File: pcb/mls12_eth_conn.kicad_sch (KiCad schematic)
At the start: 12 parts, among them J1 MTJ-88ARX1-FSM-LG

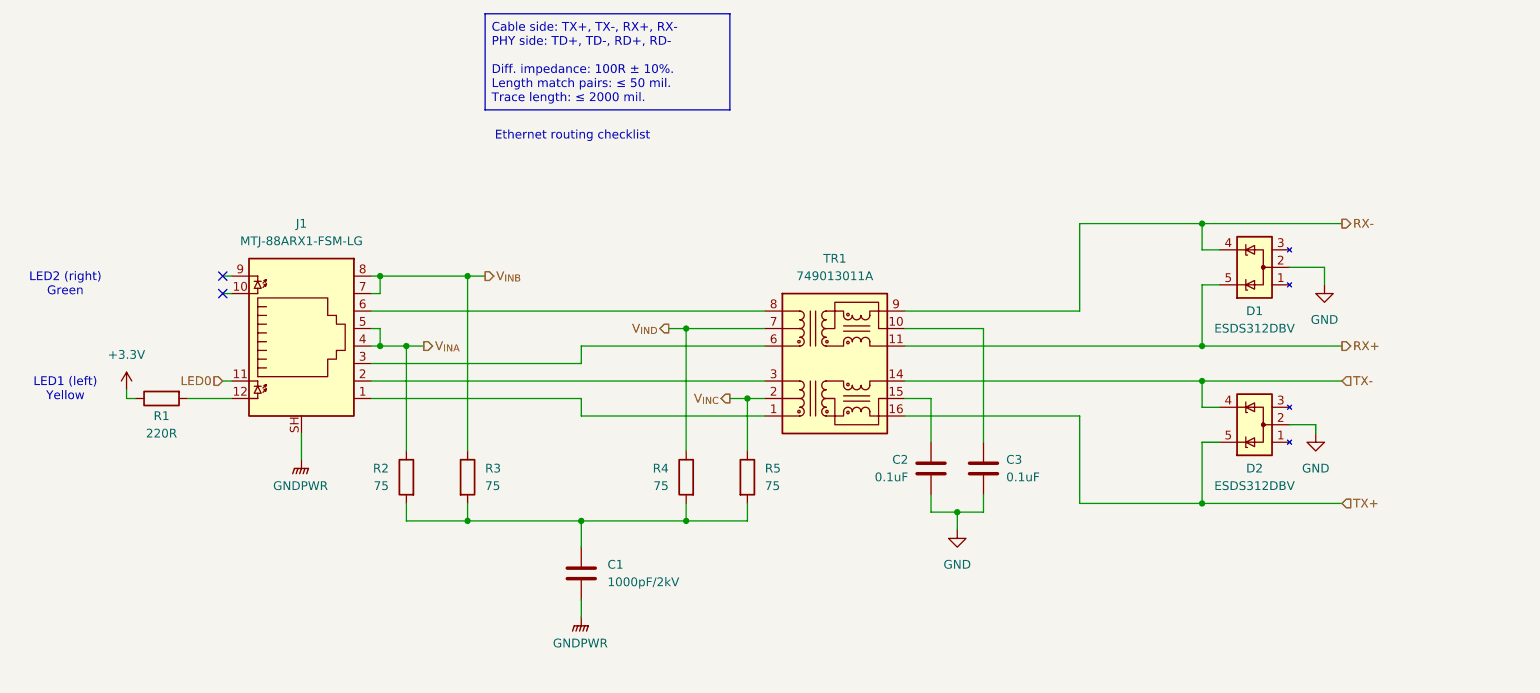
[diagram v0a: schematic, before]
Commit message: Update to 25W PoE+ module, 2 outputs
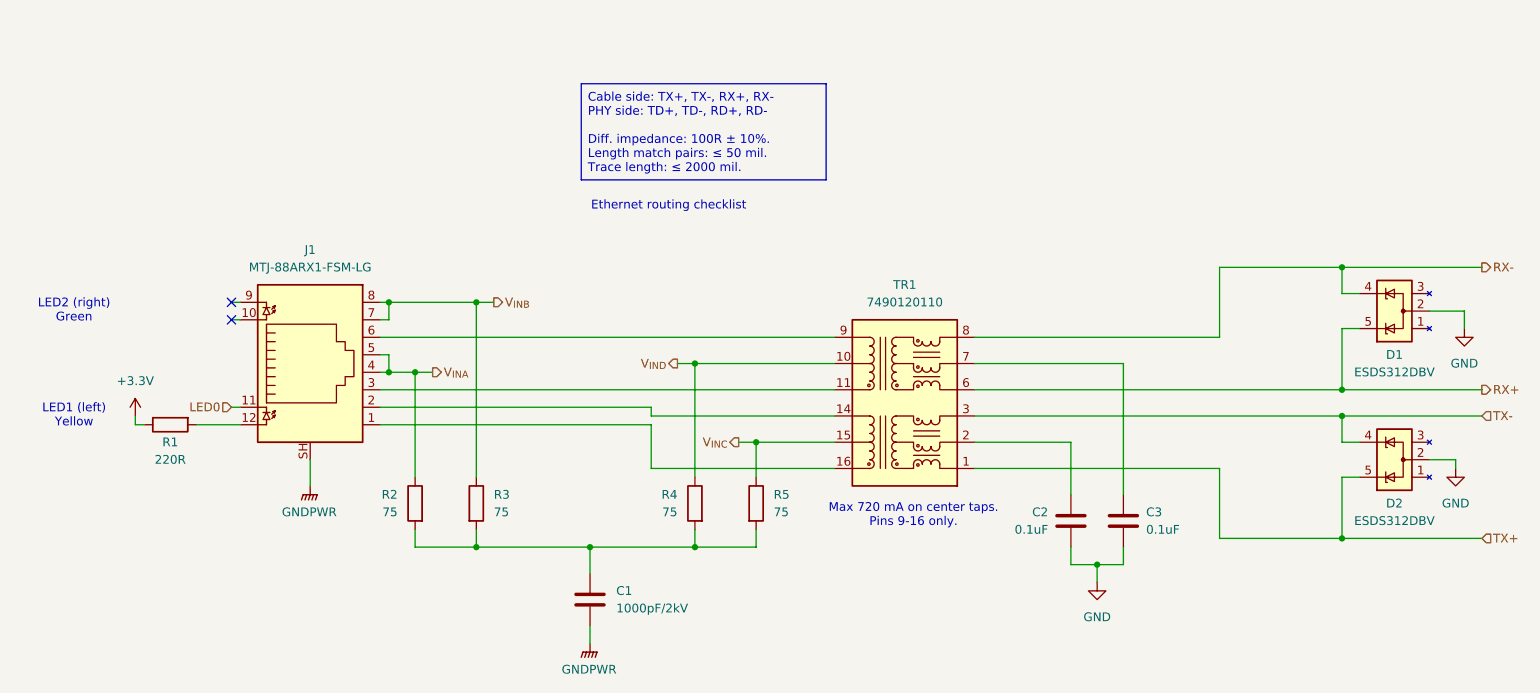
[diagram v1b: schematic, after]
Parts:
- removed TR1: 749013011A, Transformer_SMD:Transformer_Ethernet_Wuerth_749013011A, symbol Transformer:Wuerth_749013011A
- added TR1: 7490120110, symbol mls12:7490120110
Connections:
- net RX+: now also TR1.6 (RD+)
- net RX-: now also TR1.8 (RD-)
- net TX+: now also TR1.1 (TD+)
- net TX-: now also TR1.3 (TD-)
- net V_{INC}: now also TR1.15 (CTX)
- net V_{IND}: now also TR1.10 (CRX)
- net at C2.1: now also TR1.2 (CTD)
- net at C3.1: now also TR1.7 (CRD)
- net at J1.1: now also TR1.16 (TX+)
- net at J1.2: now also TR1.14 (TX-)
- net at J1.3: now also TR1.11 (RX+)
- net at J1.6: now also TR1.9 (RX-)
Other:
- note added: "Max 720 mA on center taps. Pins 9-16 only."
- company: (none) -> Quomodo BV
- moved on the sheet: C1, C2, C3, D1, D2, J1, R1, R2, R3, R4, R5

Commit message: Fix default footprint for PoE+ magnetics
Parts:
- TR1: footprint (none) -> mls12:7490120110
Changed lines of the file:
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@@
 			)
 		)
-		(property "Footprint" ""
+		(property "Footprint" "mls12:7490120110"
 			(at 163.83 82.55 0)
 			(effects

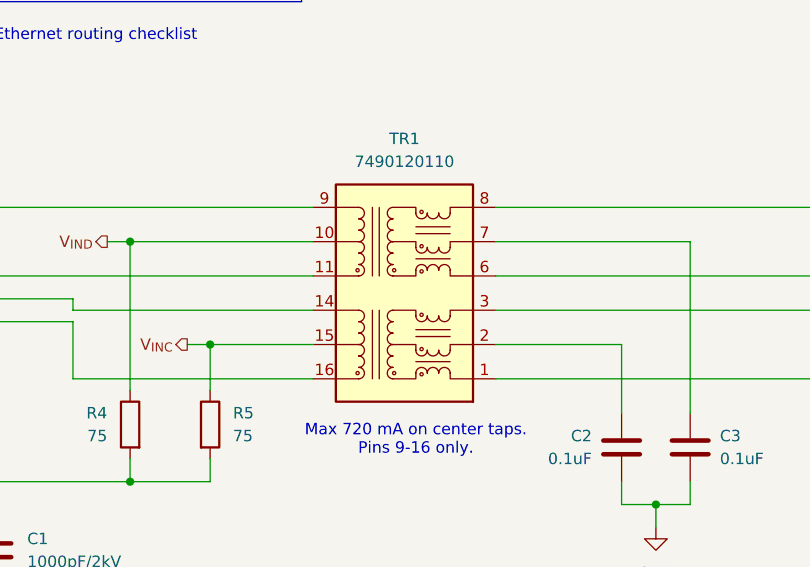
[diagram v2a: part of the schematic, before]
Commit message: First Ethernet frontend layout
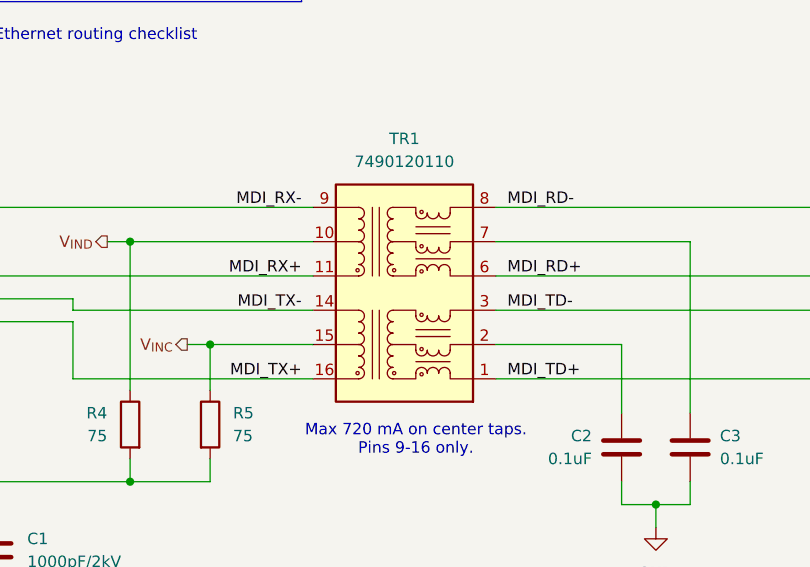
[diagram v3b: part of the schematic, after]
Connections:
- net MDI_TX+: now reaches J1.1, TR1.16 (TX+)
- net MDI_TX-: now reaches J1.2, TR1.14 (TX-)
- net MDI_RX+: now reaches J1.3, TR1.11 (RX+)
- net MDI_RX-: now reaches J1.6, TR1.9 (RX-)
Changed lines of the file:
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@@
+		)
+	)
+	(label "MDI_TD+"
+		(at 175.26 105.41 0)
+		(effects
+			(font
+				(size 1.27 1.27)
+			)
+			(justify left bottom)
+		)
+	)
+	(label "MDI_RD-"
+		(at 175.26 86.36 0)
+		(effects
+			(font
+				(size 1.27 1.27)
+			)
+			(justify left bottom)
+		)
+	)
+	(label "MDI_RD+"
+		(at 175.26 93.98 0)
+		(effects
+			(font
+				(size 1.27 1.27)
+			)
+			(justify left bottom)
+		)
+	)
+	(label "MDI_TD-"
+		(at 175.26 97.79 0)
+		(effects
+			(font
+				(size 1.27 1.27)
+			)
+			(justify left bottom)
+		)
+	)
+	(label "MDI_TX+"
+		(at 152.4 105.41 180)
+		(effects
+			(font
+				(size 1.27 1.27)
+			)
+			(justify right bottom)
+		)
+	)
+	(label "MDI_RX-"
+		(at 152.4 86.36 180)
+		(effects
+			(font
+				(size 1.27 1.27)
+			)
+			(justify right bottom)
+		)
+	)
+	(label "MDI_RX+"
+		(at 152.4 93.98 180)
+		(effects
+			(font
+				(size 1.27 1.27)
+			)
+			(justify right bottom)
+		)
+	)
+	(label "MDI_TX-"
+		(at 152.4 97.79 180)
+		(effects
+			(font
+				(size 1.27 1.27)
+			)
+			(justify right bottom)
 		)
 	)

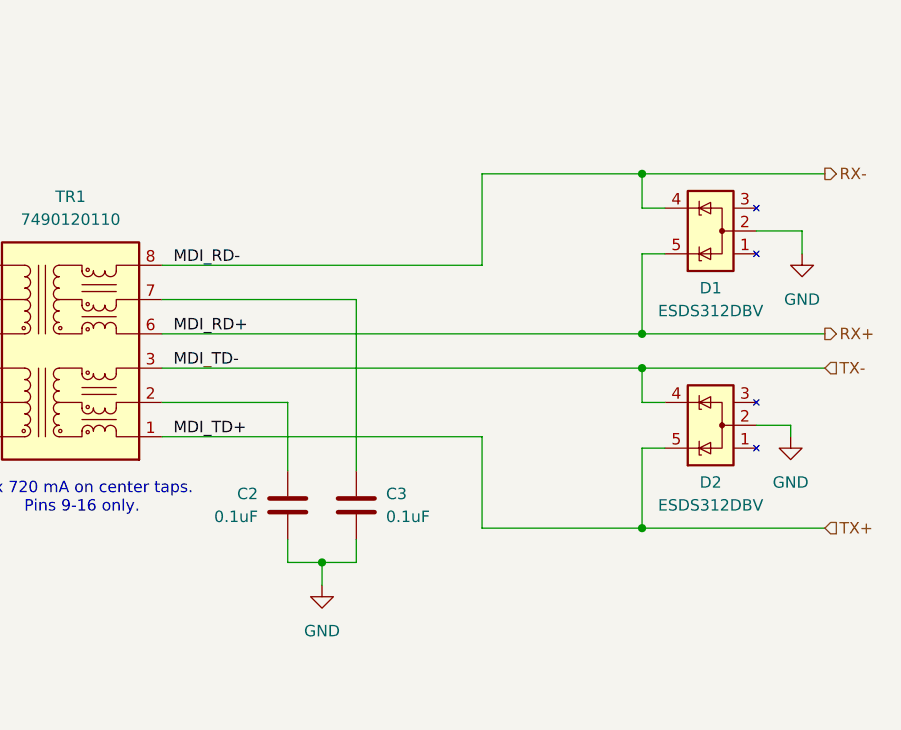
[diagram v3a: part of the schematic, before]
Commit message: Allow MDI DPs to be routed through TVS free pins
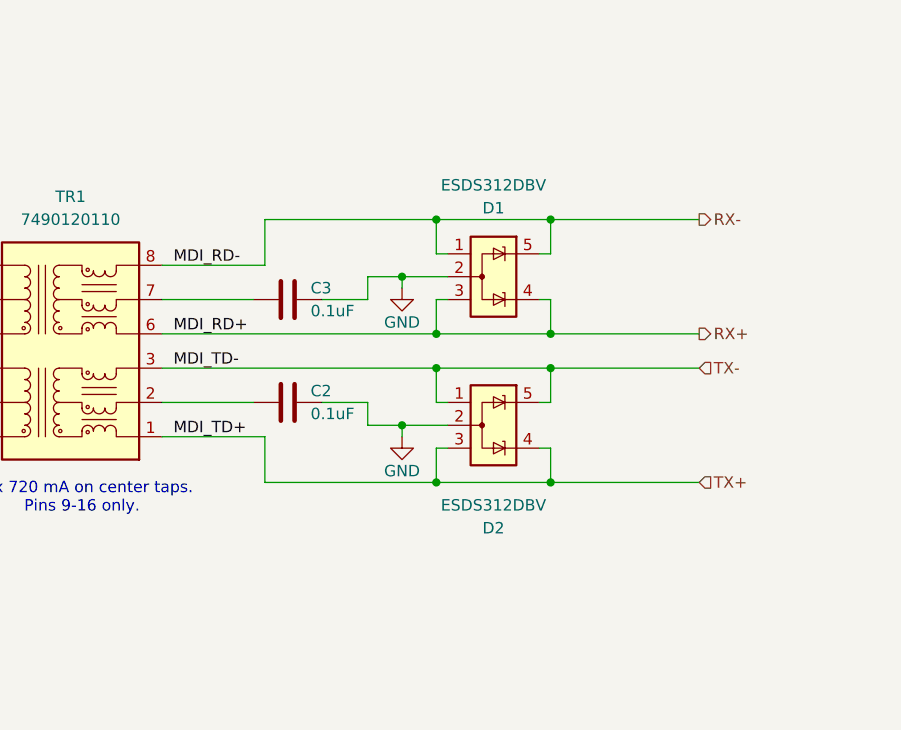
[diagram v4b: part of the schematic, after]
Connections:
- net RX+: now also D1.3 (NC), D1.4 (K); no longer D1.5 (K)
- net RX-: now also D1.1 (NC), D1.5 (K); no longer D1.4 (K)
- net TX+: now also D2.3 (NC), D2.4 (K); no longer D2.5 (K)
- net TX-: now also D2.1 (NC), D2.5 (K); no longer D2.4 (K)
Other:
- moved on the sheet: C2, C3
